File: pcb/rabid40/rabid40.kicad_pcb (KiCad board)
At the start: 2 copper layers, 285.8 x 76.2 mm, 136 parts, among them J1 SWD, J2 Conn_01x04, J3 MX_SW_solder, K1 MX_SW_solder, M1 MX_SW_solder, P1 MX_SW_solder, Q1 MX_SW_solder, SW7 SW_Push, T1 MX_SW_solder, U1 RP2040, U2 W25Q128JVS, U3 XC6206PxxxMR-Regulator_Linear, U4 MX_SW_solder, X1 MX_SW_solder, Y1 12MHz, Y2 MX_SW_solder

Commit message: added branding
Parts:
- J2: value Conn_01x04 -> JLCJLCJLCJLCJLCJLC
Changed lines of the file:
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@@
       (effects (font (size 1 1) (thickness 0.15)))
     )
-    (fp_text value "Conn_01x04" (at 3.75 2.7) (layer "F.Fab")
+    (fp_text value "JLCJLCJLCJLCJLCJLC" (at 3.75 2.7) (layer "F.Fab")
       (effects (font (size 1 1) (thickness 0.15)))
     )

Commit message: added backplane, fixed header breakout
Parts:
- J2: footprint Connector_JST:JST_EH_S4B-EH_1x04_P2.50mm_Horizontal -> Connector_JST:JST_SH_SM04B-SRSS-TB_1x04-1MP_P1.00mm_Horizontal; moved to B.Cu
- moved J1 17.9 mm to (74.0, 112.4), turned to 90 degrees
- moved R3 11.3 mm to (77.7, 109.9), turned to 180 degrees
- moved J2 4.05 mm to (116.7, 56.5)
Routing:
- net SWCLK: track 44.9 -> 18.7 mm, vias 2 -> 0
- net SWD: track 40.4 -> 20.6 mm, vias 2 -> 0
- net Col2: track 183.9 -> 168.3 mm
- net +3V3: track 135.7 -> 147.2 mm, vias 6 -> 7
- net Col3: track 151.4 -> 144.0 mm
- net ~{RESET}: track 34.9 -> 27.9 mm, vias 2 -> 0
- net Col0: track 162.6 -> 156.7 mm
- net Col1: track 173.7 -> 168.2 mm
- net GND: track 38.0 -> 41.5 mm
- net (no net): track 0.00 -> 3.54 mm, vias 0 -> 2
- net Row1: track 304.8 -> 302.4 mm
- net VBUS: track 10.2 -> 12.0 mm
- net Net-(Alt1-Pad2): track 7.94 -> 8.77 mm
- net D_N: track 13.5 -> 14.2 mm
- net Col7: track 147.2 -> 146.6 mm

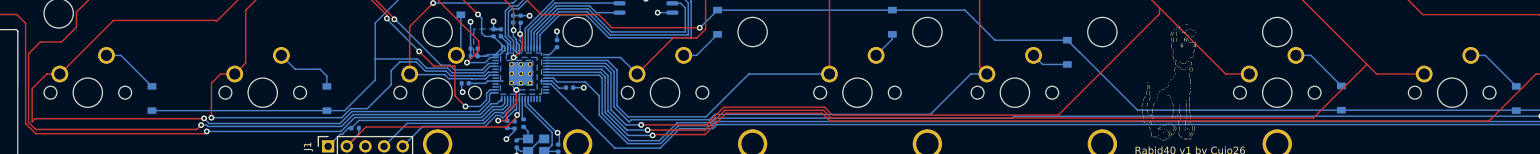
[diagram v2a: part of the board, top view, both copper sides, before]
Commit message: fixed some issues to make it manufacturable at jlcpcb
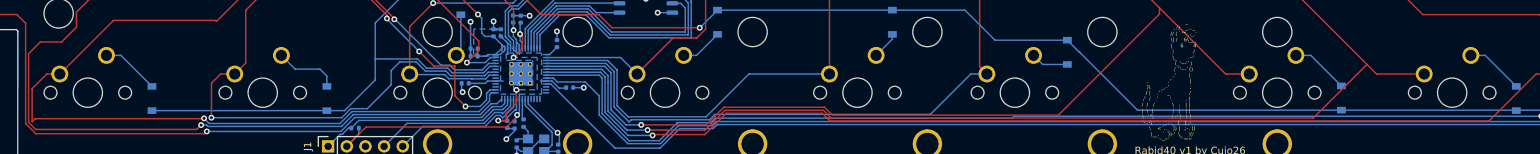
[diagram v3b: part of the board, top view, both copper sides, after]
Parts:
- J2: value JLCJLCJLCJLCJLCJLC -> Conn_01x04
- renumbered Alt1 to ALT1, Alt2 to ALT2, Bspc1 to BSPC1, Ctrl1 to CTRL1, Enter1 to ENTER1, Fn1 to FN1, LMod1 to LMOD1, RMod1 to RMOD11, Shift1 to SHIFT1, Shift2 to SHIFT2, Shift3 to SHIFT3, Space2.25 to SPACE2.25, Space2.75 to SPACE2.75, Space_7u1 to SPACE_7u1, StepCtrl1 to STEPCTRL1, Tab1 to TAB1, Win1 to WIN1, Win2 to WIN2
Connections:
- D14 pad 2: Net-(Alt1-Pad2) -> Net-(ALT1-Pad2)
- D38 pad 2: Net-(Alt2-Pad2) -> Net-(ALT2-Pad2)
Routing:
- net Net-(Alt2-Pad2): track 7.94 -> 0.00 mm
- net Net-(ALT2-Pad2): track 0.00 -> 7.94 mm
- net D_N: track 14.2 -> 16.0 mm, vias 0 -> 1
- net (no net): track 3.54 -> 1.72 mm, vias 2 -> 1

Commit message: added meme
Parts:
- added G***: LOGO, rabidgfx:reee_30mm, B.Cu at (59.0, 100.6)
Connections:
- ALT1 pad 2: Net-(Alt1-Pad2) -> Net-(ALT1-Pad2)
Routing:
- net Net-(Alt1-Pad2): track 8.77 -> 0.00 mm
- net Net-(ALT1-Pad2): track 0.00 -> 7.94 mm
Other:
- outline, holes or cut-outs redrawn

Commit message: new gerbers and drill files
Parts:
- moved G*** 50.7 mm to (28.0, 60.6)
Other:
- board text added: "Why aren't you using a 40%??? REEEEEEEEEEEEEEEEEEE"
